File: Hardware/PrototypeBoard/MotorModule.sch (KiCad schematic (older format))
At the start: 15 parts, among them J1 Conn_01x03

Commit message: Added LEDs for PWM, SPI communication, Gate Driver Errors and Gate Driver disabled
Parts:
- added D10, D5, D6, D7, D8, D9: Yellow, LEDs:LED_0805_HandSoldering, symbol Device:LED
- added D11, D3, D4: Red, LEDs:LED_0805_HandSoldering, symbol Device:LED
- added R10, R4, R5, R6, R8, R9: 560, Resistors_SMD:R_0805_HandSoldering, symbol Device:R
- added R13, R3, R7: 220, Resistors_SMD:R_0805_HandSoldering, symbol Device:R
- renumbered R3 to R11, R4 to R12, R5 to R14, R6 to R15, R7 to R16, R8 to R17, R9 to R18, R10 to R19
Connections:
- net labels added: +3.3V
- wire segments 97 -> 121

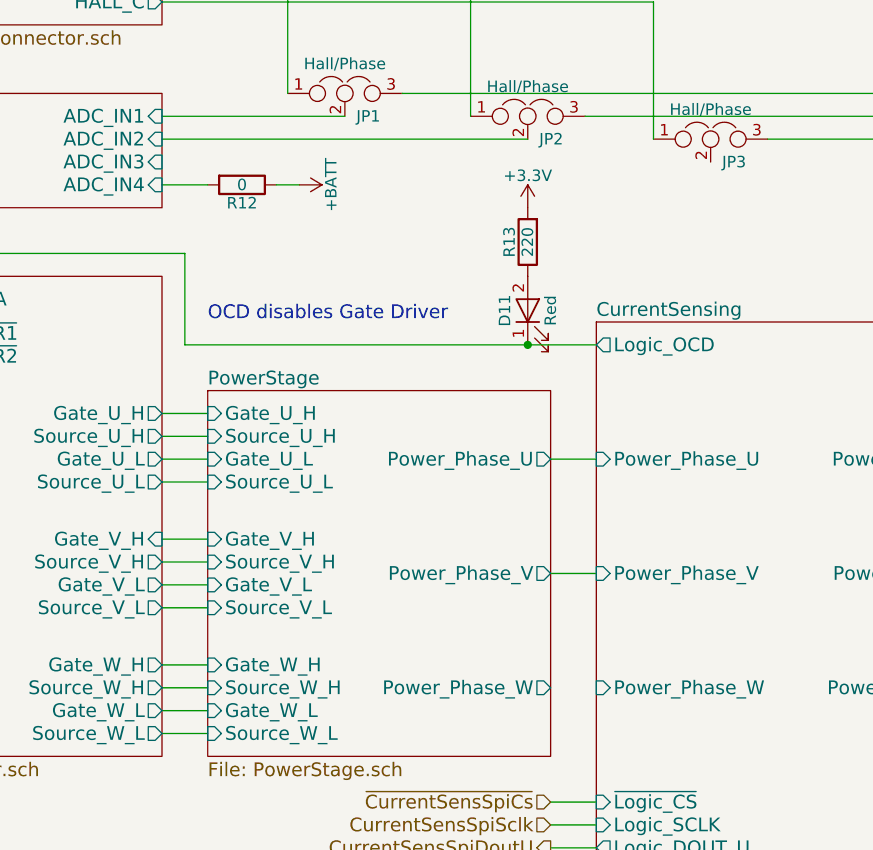
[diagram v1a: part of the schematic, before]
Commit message: All tracks routed, fixed bug in schematic, smaller test points
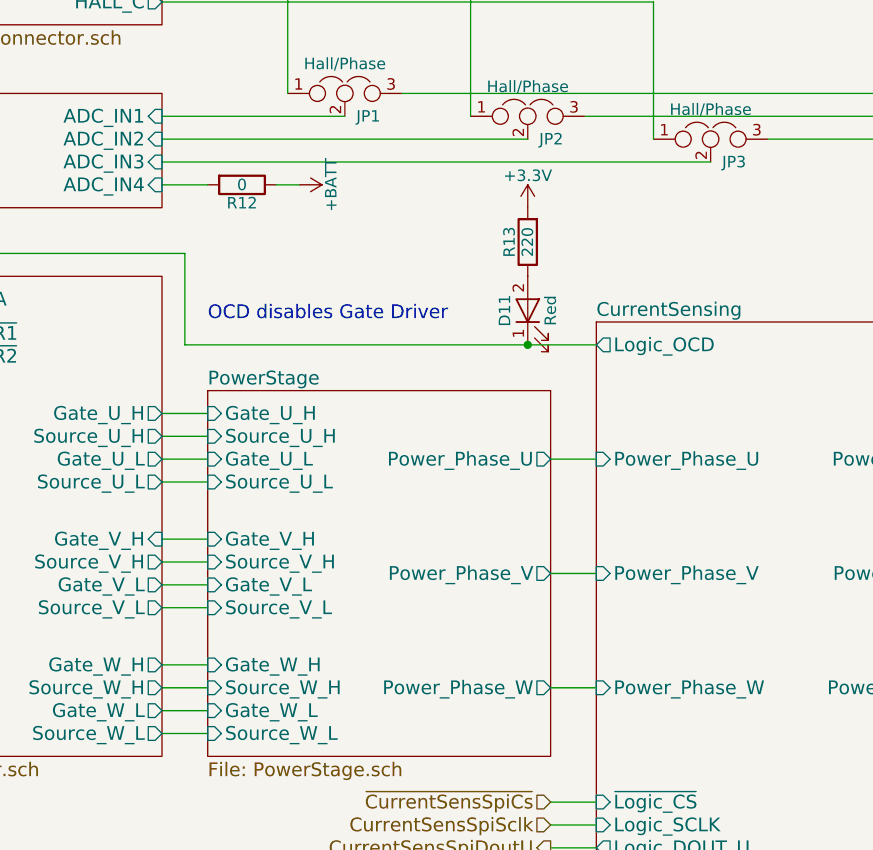
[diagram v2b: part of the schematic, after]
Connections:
- wire segments 121 -> 123
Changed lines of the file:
@@
 Wire Wire Line
 	2700 6800 2700 6100
+Wire Wire Line
+	6300 4900 6500 4900
+Wire Wire Line
+	4600 2600 7000 2600
 $EndSCHEMATC

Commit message: Some deduplication, renaming and cleanups in the schematic
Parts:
- removed C1, C2, C3: 100n, Capacitors_SMD:C_0805_HandSoldering, symbol Device:C
- removed JP1, JP2, JP3: Hall/Phase, Connectors:GS3, symbol Device:Jumper_NC_Dual
- removed R14, R16, R18: 1.5k, Resistors_SMD:R_0805_HandSoldering, symbol Device:R
- removed R15, R17, R19: DNP, Resistors_SMD:R_0805_HandSoldering, symbol Device:R
- added C? (x2): 220μF, 50V, Capacitors_SMD:CP_Elec_10x10, symbol Device:CP
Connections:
- net labels added: GNDPWR, ~LogicOverCurrent
- net labels removed: GND
- wire segments 123 -> 132
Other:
- note added: "DC-Link capacitors"
- note added: "Power Consumption estimation 3.3V Rail:\nEncoder: 15mA (AMS5048)\nADC: 1mA\nLEDs: 6x10mA\nGateDriver: 0mA (no 3.3V supply)\nCurrent Sensors: 3x20mA (maximum)\n\nTotal: 136mA"
- note removed: "1kHz low pass"
- note removed: "Power Consumption estimation 3.3V Rail:\nEncoder: 15mA (AMS5048)\nADC: 1mA\nGateDriver: 0mA (no 3.3V supply)\nCurrent Sensors: 3x20mA (maximum)\n\nTotal: 76mA"
- moved on the sheet: D10, D11, D3, D4, D5, D6, D7, D8, D9, R10, R11, R12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
